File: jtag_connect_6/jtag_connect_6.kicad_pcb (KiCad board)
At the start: 2 copper layers, 46 x 18 mm, 2 parts, among them J1 jtag-connect-6, J2 Conn_01x06_Pin

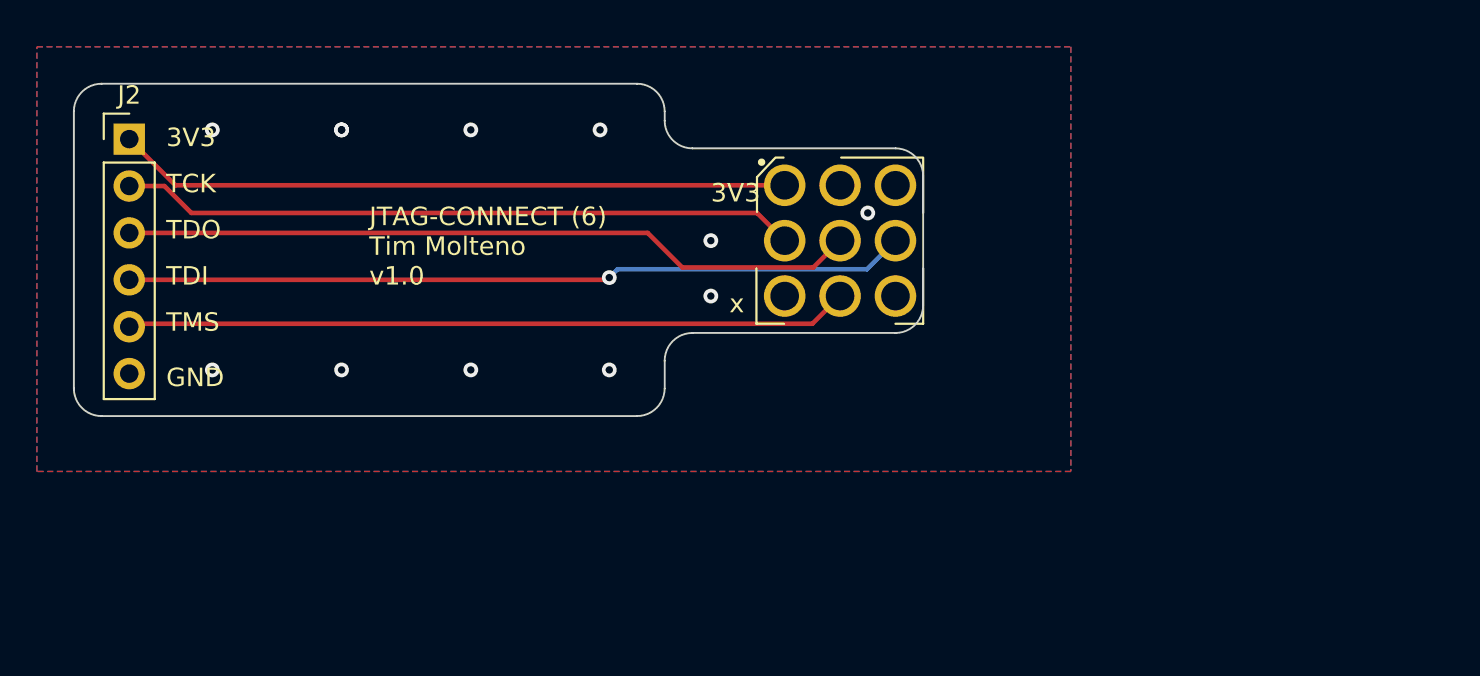
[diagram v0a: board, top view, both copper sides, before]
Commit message: Better size and new pins for JTAG
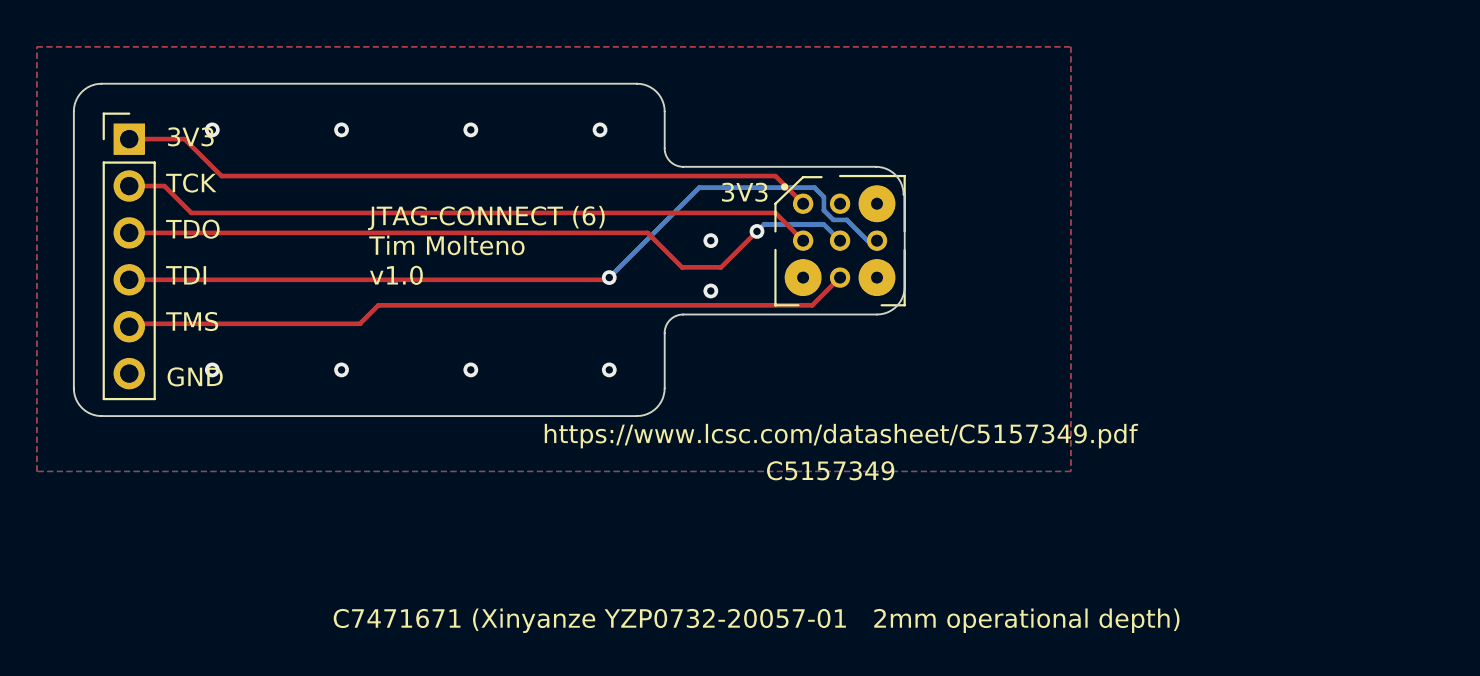
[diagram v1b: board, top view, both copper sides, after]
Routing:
- net Net-(J1-TDI): track 42.4 -> 44.2 mm
- net Net-(J1-3V3): track 36.5 -> 37.9 mm
- net Net-(J1-TCK): track 36.7 -> 37.7 mm
- net Net-(J1-TDO): track 39.9 -> 40.6 mm, vias 0 -> 1
- net GND: vias 12 -> 10
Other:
- board size 46 x 18 mm -> 45 x 18 mm
- board text removed: "x"

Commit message: Update JTAG to use plated through holes for strength. Also use Sipeed RV Debugger pinout
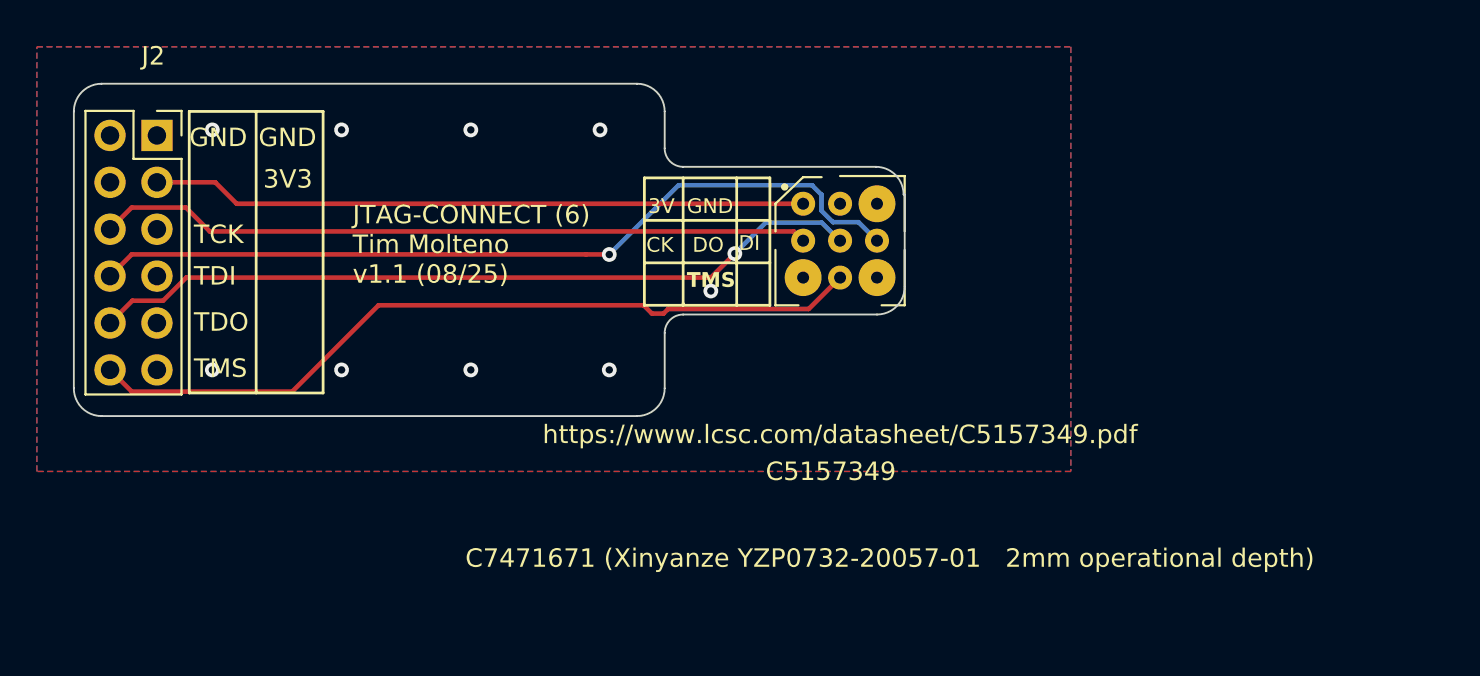
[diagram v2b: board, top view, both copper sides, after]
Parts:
- J2: value Conn_01x06_Pin -> Conn_02x06_Odd_Even; footprint Connector_PinHeader_2.54mm:PinHeader_1x06_P2.54mm_Vertical -> Connector_PinSocket_2.54mm:PinSocket_2x06_P2.54mm_Vertical
- moved J2 1.51 mm to (120.5, 63.8)
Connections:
- J1 pad 1: Net-(J1-3V3) -> +3V3
- J1 pad 3: Net-(J1-TCK) -> JTAG_TCK
- J1 pad 4: Net-(J1-TDO) -> JTAG_TDO
- J1 pad 5: Net-(J1-TDI) -> JTAG_TDI
- J1 pad 6: Net-(J1-TMS) -> JTAG_TMS
- J2 pad 1: Net-(J1-3V3) -> GND
- J2 pad 2: Net-(J1-TCK) -> GND
- J2 pad 3: Net-(J1-TDO) -> +3V3
- J2 pad 4: Net-(J1-TDI) -> unconnected-(J2-Pin_4-Pad4)
- J2 pad 5: Net-(J1-TMS) -> unconnected-(J2-Pin_5-Pad5)
- J2 pad 6: GND -> JTAG_TCK
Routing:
- net JTAG_TDI: track 0.00 -> 45.3 mm, vias 0 -> 1
- net Net-(J1-TDI): track 44.2 -> 0.00 mm, vias 1 -> 0
- net JTAG_TMS: track 0.00 -> 43.0 mm
- net JTAG_TDO: track 0.00 -> 42.2 mm, vias 0 -> 1
- net Net-(J1-TDO): track 40.6 -> 0.00 mm, vias 1 -> 0
- net Net-(J1-TMS): track 39.6 -> 0.00 mm
- net JTAG_TCK: track 0.00 -> 38.8 mm
- net Net-(J1-3V3): track 37.9 -> 0.00 mm
- net Net-(J1-TCK): track 37.7 -> 0.00 mm
- net +3V3: track 0.00 -> 35.5 mm
- net GND: vias 10 -> 9
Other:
- board text added: "3V"
- board text added: "CK"
- board text added: "DI"
- board text added: "DO"
- board text added: "JTAG-CONNECT (6) Tim Molteno v1.1 (08/25)"
- board text removed: "JTAG-CONNECT (6) Tim Molteno v1.0"
